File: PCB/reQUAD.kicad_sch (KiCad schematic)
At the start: 13 parts, among them J1 Model_100_System_BUS, U1 AS6C1008, U2 HC573, U3 2G79, U4 HC02

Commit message: improve hand-solderability of TSSOP parts
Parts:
- BT1: MPN (none) -> Keystone 3031
- DA1: MPN (none) -> BAV756S,115
- U1: MPN (none) -> AS6C1008-55STIN
- U2: MPN (none) -> 74AHC573PW,118
- U3: MPN (none) -> SN74LVC2G79DCTR
- U4: MPN (none) -> 74HC02PW,118
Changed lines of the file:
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@@
 	(title_block
 		(title "reQUAD")
-		(date "2023-10-18")
-		(rev "023")
+		(date "2024-11-21")
+		(rev "024")
 		(company "Brian K. White - b.kenyon.w@gmail.com")
 		(comment 1 "Original Design: Steve Adolph")
@@
 			)
 		)
-		(property "Datasheet" "datasheets/74AHC02.pdf"
+		(property "Datasheet" "datasheets/HC02.pdf"
 			(at 119.38 127 0)
 			(effects
@@
 			)
 		)
-		(property "Description" ""
+		(property "Description" "IC GATE NOR 4CH 2-INP 14TSSOP"
+			(at 119.38 127 0)
+			(effects
+				(font
+					(size 1.27 1.27)
+				)
+				(hide yes)
+			)
+		)
+		(property "MPN" "74HC02PW,118"
 			(at 119.38 127 0)
 			(effects
@@
 			)
 		)
-		(property "Datasheet" "datasheets/74AHC02.pdf"
+		(property "Datasheet" "datasheets/HC02.pdf"
 			(at 104.14 127 0)
 			(effects
@@
 			)
 		)
-		(property "Description" ""
+		(property "Description" "IC GATE NOR 4CH 2-INP 14TSSOP"
+			(at 104.14 127 0)
+			(effects
+				(font
+					(size 1.27 1.27)
+				)
+				(hide yes)
+			)
+		)
+		(property "MPN" "74HC02PW,118"
 			(at 104.14 127 0)
 			(effects
@@
 			)
 		)
-		(property "Datasheet" "datasheets/74AHC02.pdf"
+		(property "Datasheet" "datasheets/HC02.pdf"
 			(at 119.38 149.86 0)
 			(effects
@@
 			)
 		)
-		(property "Description" ""
+		(property "Description" "IC GATE NOR 4CH 2-INP 14TSSOP"
+			(at 119.38 149.86 0)
+			(effects
+				(font
+					(size 1.27 1.27)
+				)
+				(hide yes)
+			)
+		)
+		(property "MPN" "74HC02PW,118"
 			(at 119.38 149.86 0)
 			(effects
@@
 			)
 		)
-		(property "Datasheet" "datasheets/74AHC02.pdf"
+		(property "Datasheet" "datasheets/HC02.pdf"
 			(at 104.14 147.32 0)
 			(effects
@@
 			)
 		)
-		(property "Description" ""
+		(property "Description" "IC GATE NOR 4CH 2-INP 14TSSOP"
+			(at 104.14 147.32 0)
+			(effects
+				(font
+					(size 1.27 1.27)
+				)
+				(hide yes)
+			)
+		)
+		(property "MPN" "74HC02PW,118"
 			(at 104.14 147.32 0)
 			(effects
@@
 			)
 		)
-		(property "Description" ""
+		(property "Description" "IC SRAM 1Mx8 PARALLEL 5V 32STSOP"
+			(at 215.9 77.47 0)
+			(effects
+				(font
+					(size 1.27 1.27)
+				)
+				(hide yes)
+			)
+		)
+		(property "MPN" "AS6C1008-55STIN"
 			(at 215.9 77.47 0)
 			(effects
@@
 			)
 		)
-		(property "Datasheet" "datasheets/74AHC02.pdf"
+		(property "Datasheet" "datasheets/HC02.pdf"
 			(at 88.9 184.15 0)
 			(effects
@@
 			)
 		)
-		(property "Description" ""
+		(property "Description" "IC GATE NOR 4CH 2-INP 14TSSOP"
+			(at 88.9 184.15 0)
+			(effects
+				(font
+					(size 1.27 1.27)
+				)
+				(hide yes)
+			)
+		)
+		(property "MPN" "74HC02PW,118"
 			(at 88.9 184.15 0)
 			(effects
@@
 			)
 		)
-		(property "Datasheet" "datasheets/74AHC573.pdf"
+		(property "Datasheet" "datasheets/HC573.pdf"
 			(at 158.75 60.96 0)
 			(effects
@@
 			)
 		)
-		(property "Description" ""
+		(property "Description" "IC D-TYPE TRANSP SGL 8:8 20TSSOP"
+			(at 158.75 60.96 0)
+			(effects
+				(font
+					(size 1.27 1.27)
+				)
+				(hide yes)
+			)
+		)
+		(property "MPN" "74AHC573PW,118"
 			(at 158.75 60.96 0)
 			(effects
@@
 			)
 		)
-		(property "Datasheet" "datasheets/74LVC2G79.pdf"
+		(property "Datasheet" "datasheets/2G79.pdf"
 			(at 158.75 92.71 0)
 			(effects
@@
 			)
 		)
-		(property "Description" ""
+		(property "Description" "IC FF D-TYPE DUAL 1BIT SM8"
+			(at 158.75 92.71 0)
+			(effects
+				(font
+					(size 1.27 1.27)
+				)
+				(hide yes)
+			)
+		)
+		(property "MPN" "SN74LVC2G79DCTR"
 			(at 158.75 92.71 0)
 			(effects
@@
 			)
 		)
-		(property "Datasheet" "datasheets/74LVC2G79.pdf"
+		(property "Datasheet" "datasheets/2G79.pdf"
 			(at 158.75 102.87 0)
 			(effects
@@
 			)
 		)
-		(property "Description" ""
+		(property "Description" "IC FF D-TYPE DUAL 1BIT SM8"
+			(at 158.75 102.87 0)
+			(effects
+				(font
+					(size 1.27 1.27)
+				)
+				(hide yes)
+			)
+		)
+		(property "MPN" "SN74LVC2G79DCTR"
 			(at 158.75 102.87 0)
 			(effects
@@
 			)
 		)
-		(property "Datasheet" "datasheets/74LVC2G79.pdf"
+		(property "Datasheet" "datasheets/2G79.pdf"
 			(at 101.6 184.15 0)
 			(effects
@@
 			)
 		)
-		(property "Description" ""
+		(property "Description" "IC FF D-TYPE DUAL 1BIT SM8"
+			(at 101.6 184.15 0)
+			(effects
+				(font
+					(size 1.27 1.27)
+				)
+				(hide yes)
+			)
+		)
+		(property "MPN" "SN74LVC2G79DCTR"
 			(at 101.6 184.15 0)
 			(effects
@@
 			)
 		)
-		(property "Description" ""
+		(property "Description" "DIODE ARRAY GP 90V 250MA 6TSSOP"
+			(at 39.37 177.8 0)
+			(effects
+				(font
+					(size 1.27 1.27)
+				)
+				(hide yes)
+			)
+		)
+		(property "MPN" "BAV756S,115"
 			(at 39.37 177.8 0)
 			(effects
@@
 			)
 		)
-		(property "Description" ""
+		(property "Description" "DIODE ARRAY GP 90V 250MA 6TSSOP"
+			(at 46.99 182.88 0)
+			(effects
+				(font
+					(size 1.27 1.27)
+				)
+				(hide yes)
+			)
+		)
+		(property "MPN" "BAV756S,115"
 			(at 46.99 182.88 0)
 			(effects
@@
 			)
 		)
-		(property "Description" ""
+		(property "Description" "Battery Retainer Coin, 10.0mm 1 Cell PC Pin"
+			(at 54.61 187.96 0)
+			(effects
+				(font
+					(size 1.27 1.27)
+				)
+				(hide yes)
+			)
+		)
+		(property "MPN" "Keystone 3031"
 			(at 54.61 187.96 0)
 			(effects

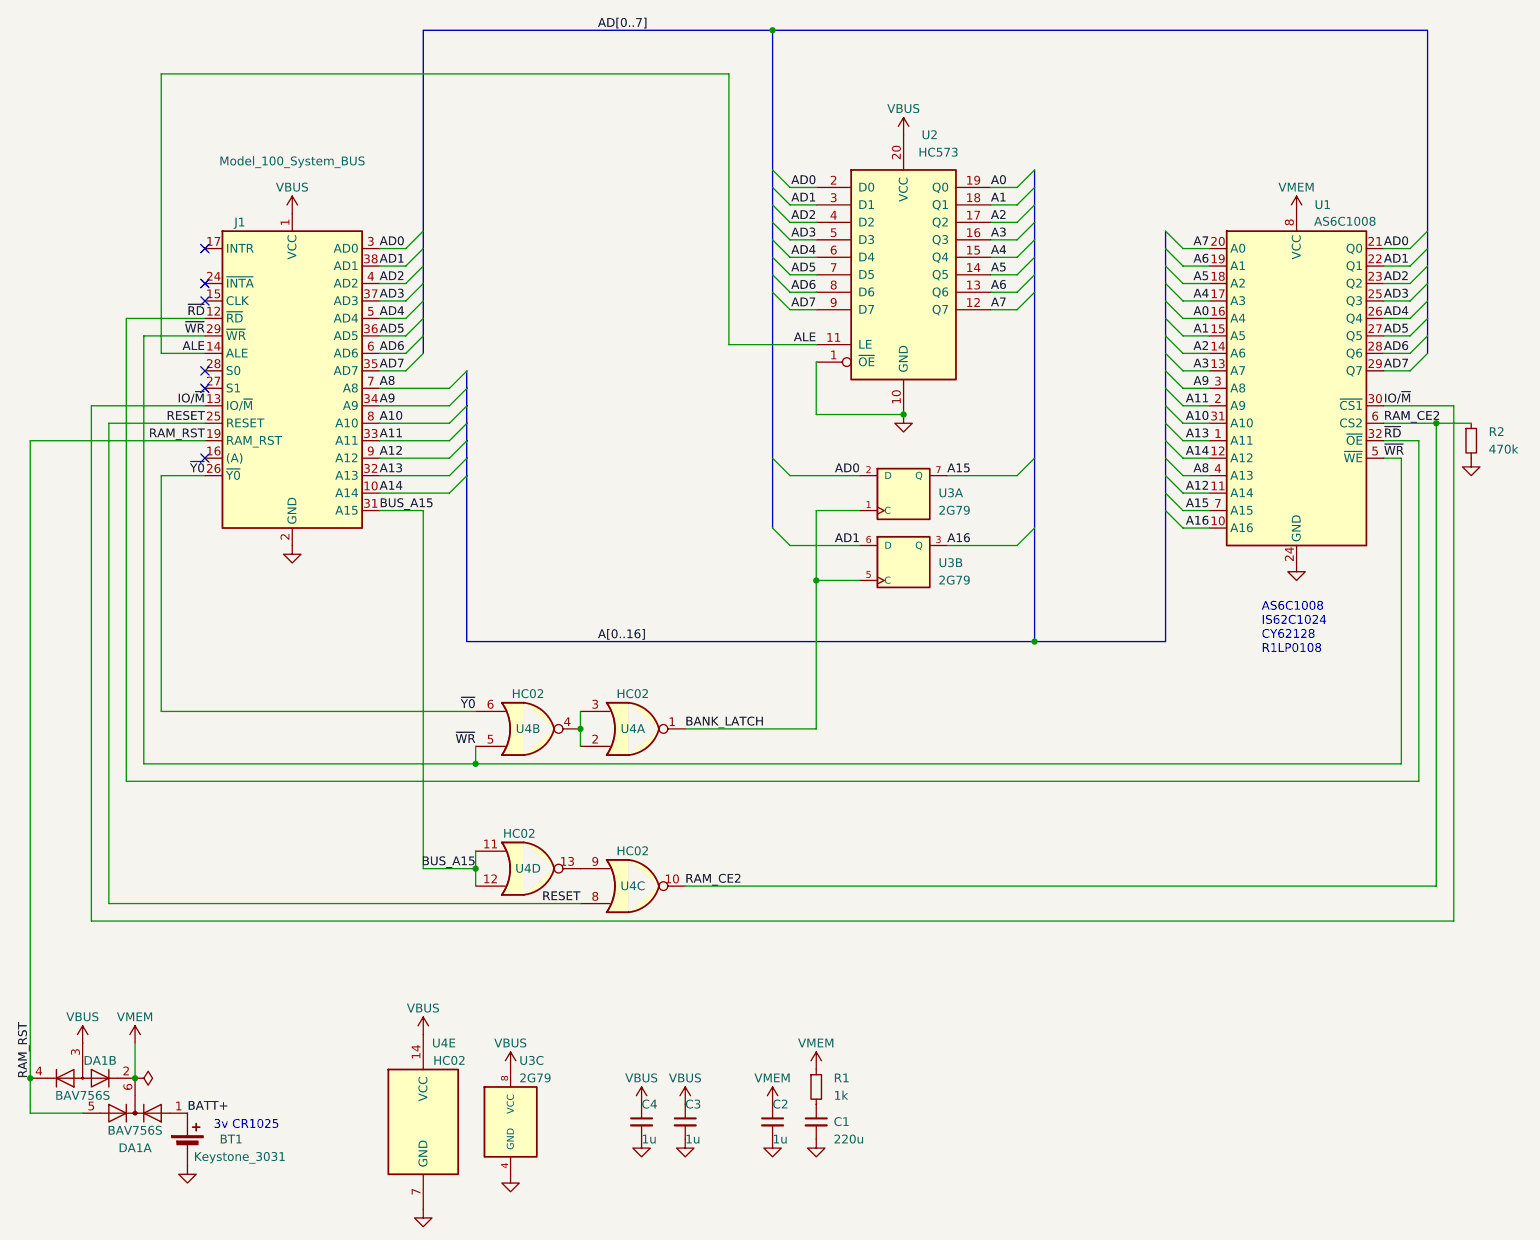
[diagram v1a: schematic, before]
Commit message: TSSOP footprints, silkscreen, MPN & bom export from sch, centroid export
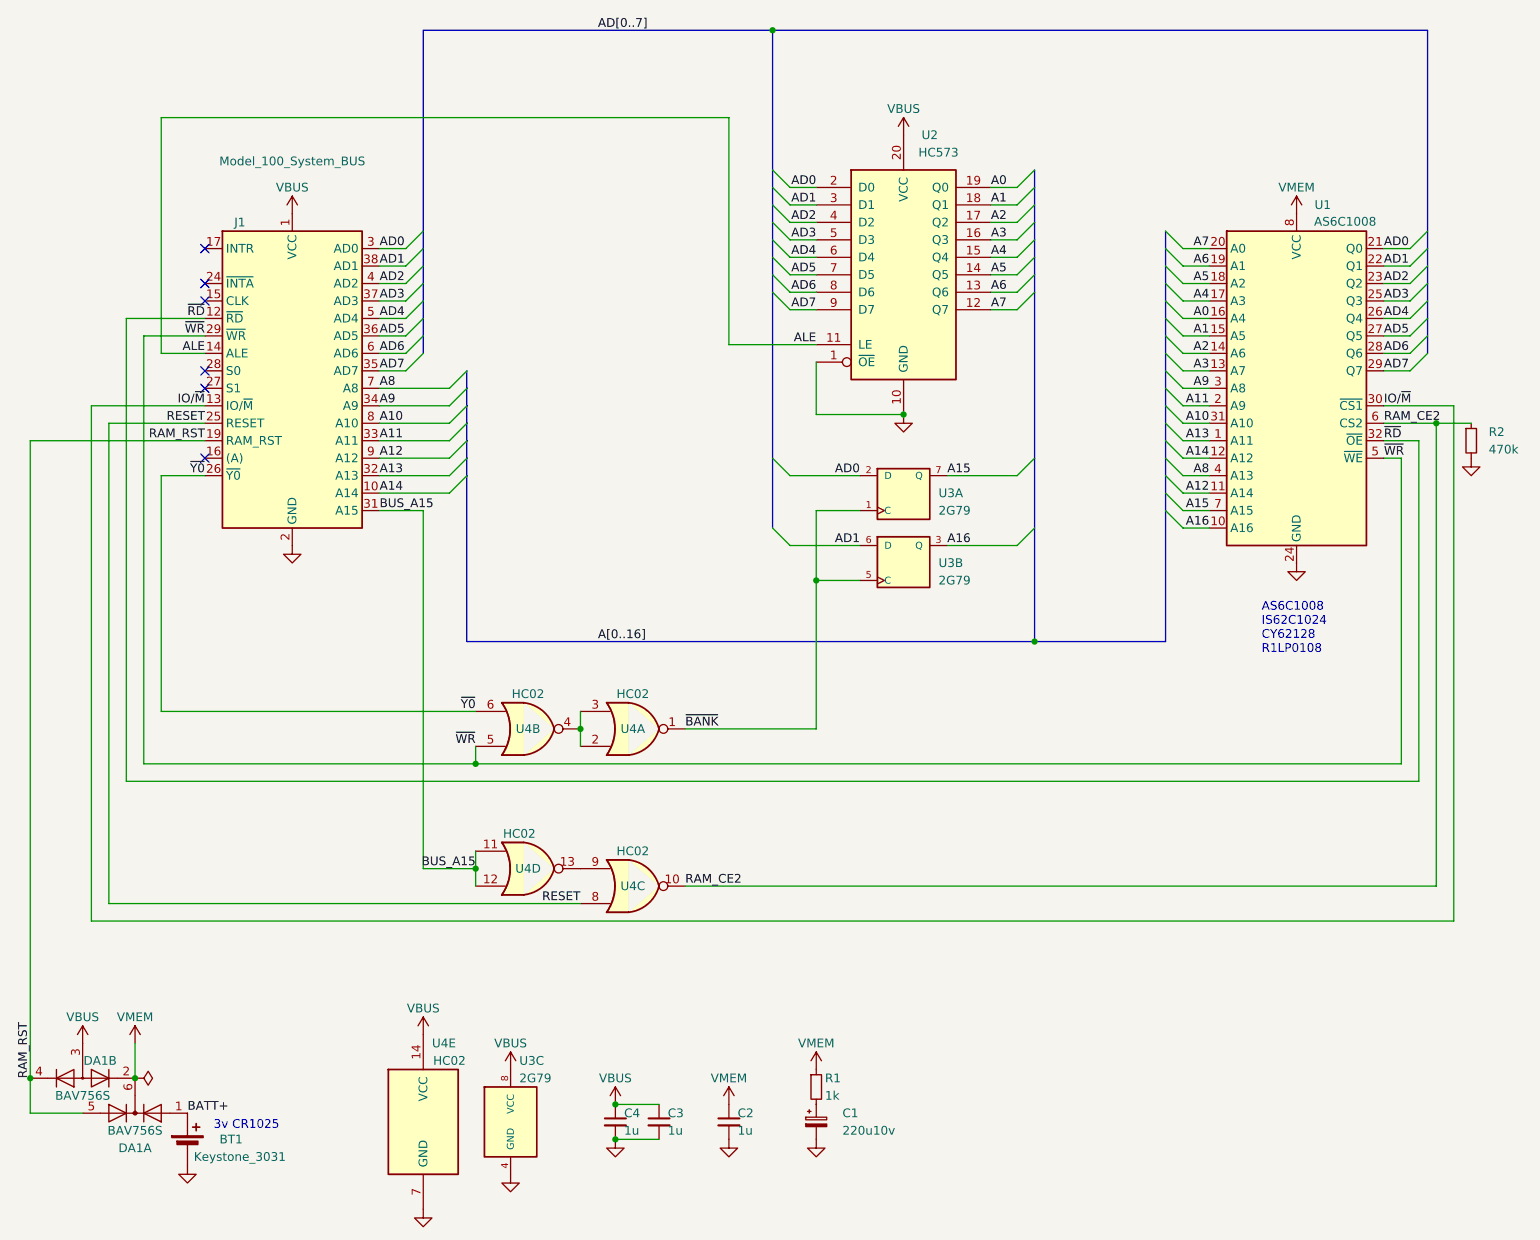
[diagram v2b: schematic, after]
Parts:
- removed C1: 220u, 000_LOCAL:CP_EIA-6032-28, symbol 000_LOCAL:C
- added C1: 220u10v, 000_LOCAL:CP_6032, symbol 000_LOCAL:C_Polarized
- C2, C3, C4: MPN (none) -> CL21B105KAFNNNE
- J1: MPN (none) -> 920-0172-01
- R1: MPN (none) -> RK73B2ATTD102J
- R2: MPN (none) -> RC0805FR-07470KL
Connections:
- net GND: now also C1.2
- net at R1.2: now also C1.1
- net BANK_LATCH renamed ~{BANK}

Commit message: 028 - tsop32 footprint
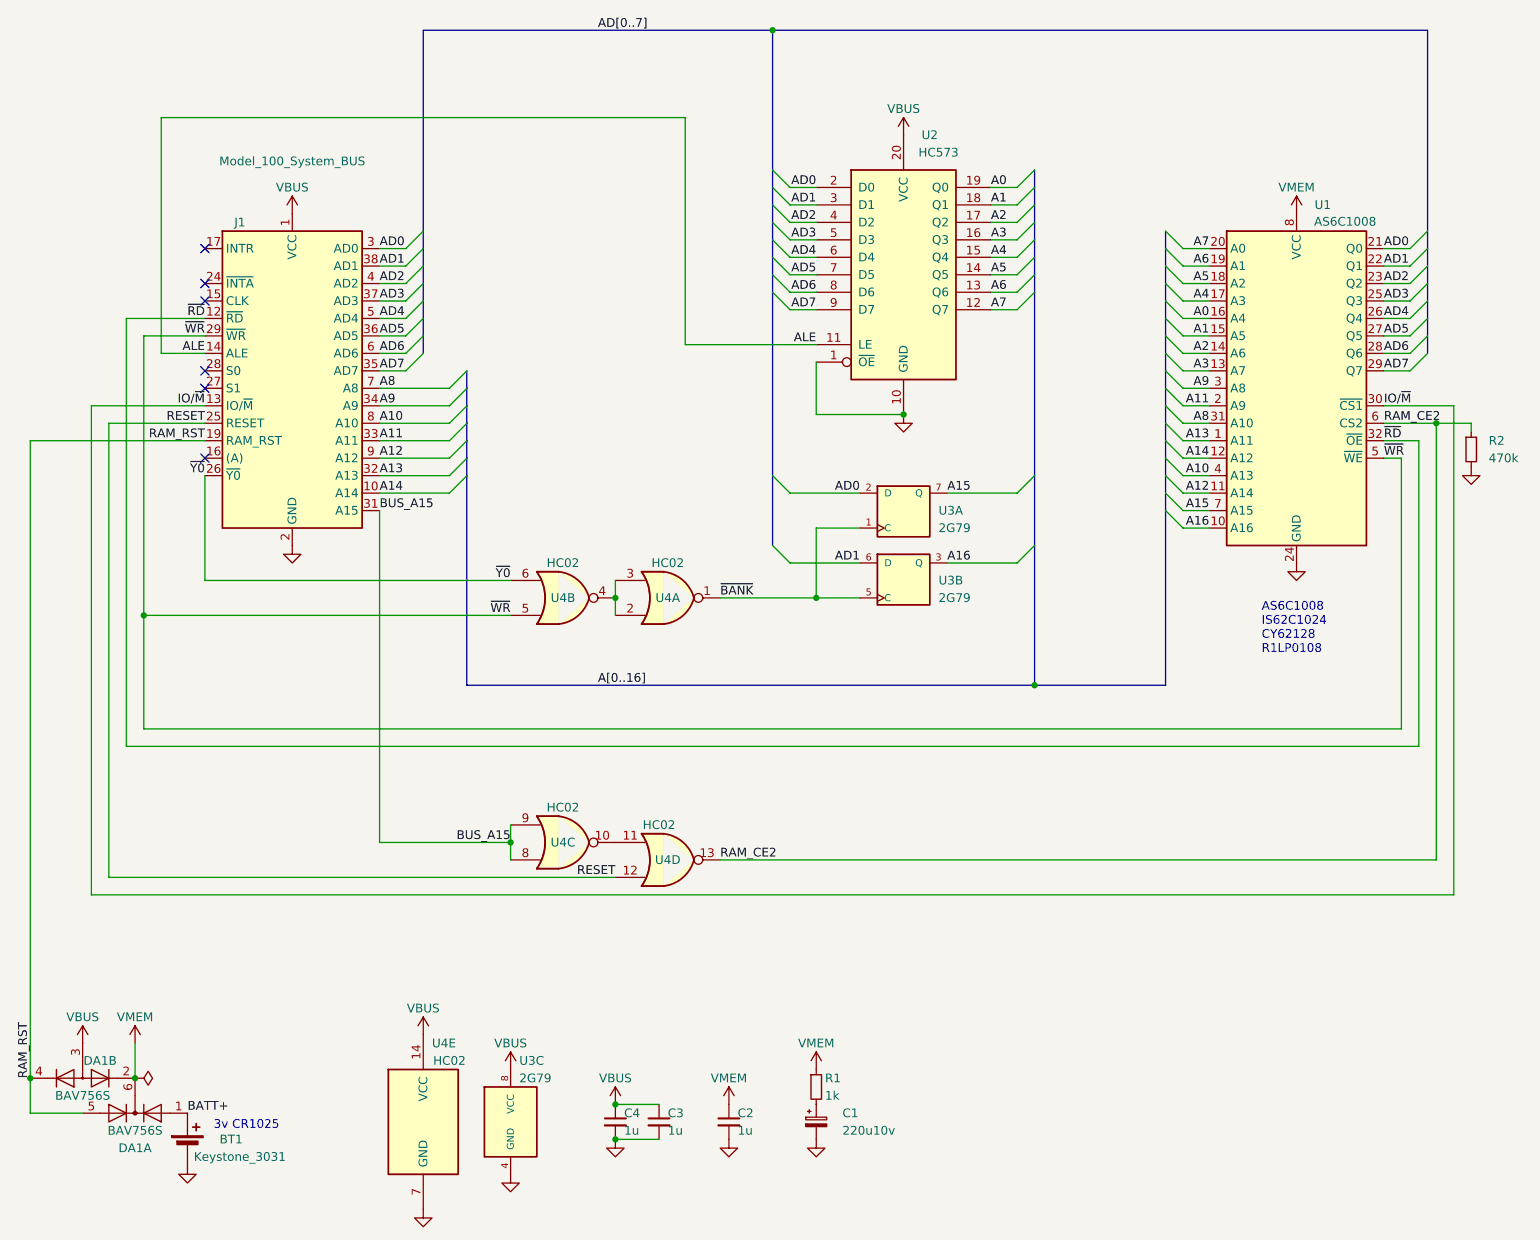
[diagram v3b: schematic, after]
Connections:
- net A10: now also U1.4 (A13); no longer U1.31 (A10)
- net A8: now also U1.31 (A10); no longer U1.4 (A13)
- net BUS_A15: now also U4.8, U4.9; no longer U4.11, U4.12
- net RAM_CE2: now also U4.13; no longer U4.10
- net RESET: now also U4.12; no longer U4.8
- new net: U4.10, U4.11
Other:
- moved on the sheet: R2, U3A, U3B, U4A, U4B, U4C, U4D

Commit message: correct MPN for VSSOP-8 package 2G79
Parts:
- U2: MPN 74AHC573PW,118 -> 74HC573PW,118
- U3: MPN SN74LVC2G79DCTR -> SN74LVC2G79DCUR
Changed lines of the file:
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@@
 			)
 		)
-		(property "MPN" "74AHC573PW,118"
+		(property "MPN" "74HC573PW,118"
 			(at 158.75 60.96 0)
 			(effects
@@
 			)
 		)
-		(property "Description" "IC FF D-TYPE DUAL 1BIT SM8"
+		(property "Description" "Flip Flop 2 Element D-Type 1 Bit Positive Edge 8-VFSOP (0.091\", 2.30mm Width)"
 			(at 158.75 95.25 0)
 			(effects
@@
 			)
 		)
-		(property "MPN" "SN74LVC2G79DCTR"
+		(property "MPN" "SN74LVC2G79DCUR"
 			(at 158.75 95.25 0)
 			(effects
@@
 			)
 		)
-		(property "Description" "IC FF D-TYPE DUAL 1BIT SM8"
+		(property "Description" "Flip Flop 2 Element D-Type 1 Bit Positive Edge 8-VFSOP (0.091\", 2.30mm Width)"
 			(at 158.75 105.41 0)
 			(effects
@@
 			)
 		)
-		(property "MPN" "SN74LVC2G79DCTR"
+		(property "MPN" "SN74LVC2G79DCUR"
 			(at 158.75 105.41 0)
 			(effects
@@
 			)
 		)
-		(property "Description" "IC FF D-TYPE DUAL 1BIT SM8"
+		(property "Description" "Flip Flop 2 Element D-Type 1 Bit Positive Edge 8-VFSOP (0.091\", 2.30mm Width)"
 			(at 101.6 184.15 0)
 			(effects
@@
 			)
 		)
-		(property "MPN" "SN74LVC2G79DCTR"
+		(property "MPN" "SN74LVC2G79DCUR"
 			(at 101.6 184.15 0)
 			(effects
